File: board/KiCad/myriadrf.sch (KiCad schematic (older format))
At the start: 1 part, among them J1 FX10B_80S_8

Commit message: First pmod side wiring
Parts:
- J1: footprint FX10B_80S_8 -> (none)
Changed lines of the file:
@@
 LIBS:ice40_1k4k_tq144
 LIBS:myriad
+LIBS:pmod
+LIBS:LMS6002-Pmod-cache
 EELAYER 25 0
 EELAYER END
@@
 F 0 "J1" H 5600 6687 60  0000 C CNN
 F 1 "FX10B_80S_8" H 5580 6720 60  0001 C CNN
-F 2 "FX10B_80S_8" H 5590 6840 60  0001 C CNN
+F 2 "" H 5590 6840 60  0001 C CNN
 F 3 "" H 5600 3750 60  0000 C CNN
 F 4 "CONN RECEPT, 80POS, W/O, POST, SMD," H 5630 6950 60  0001 C CNN "Description"

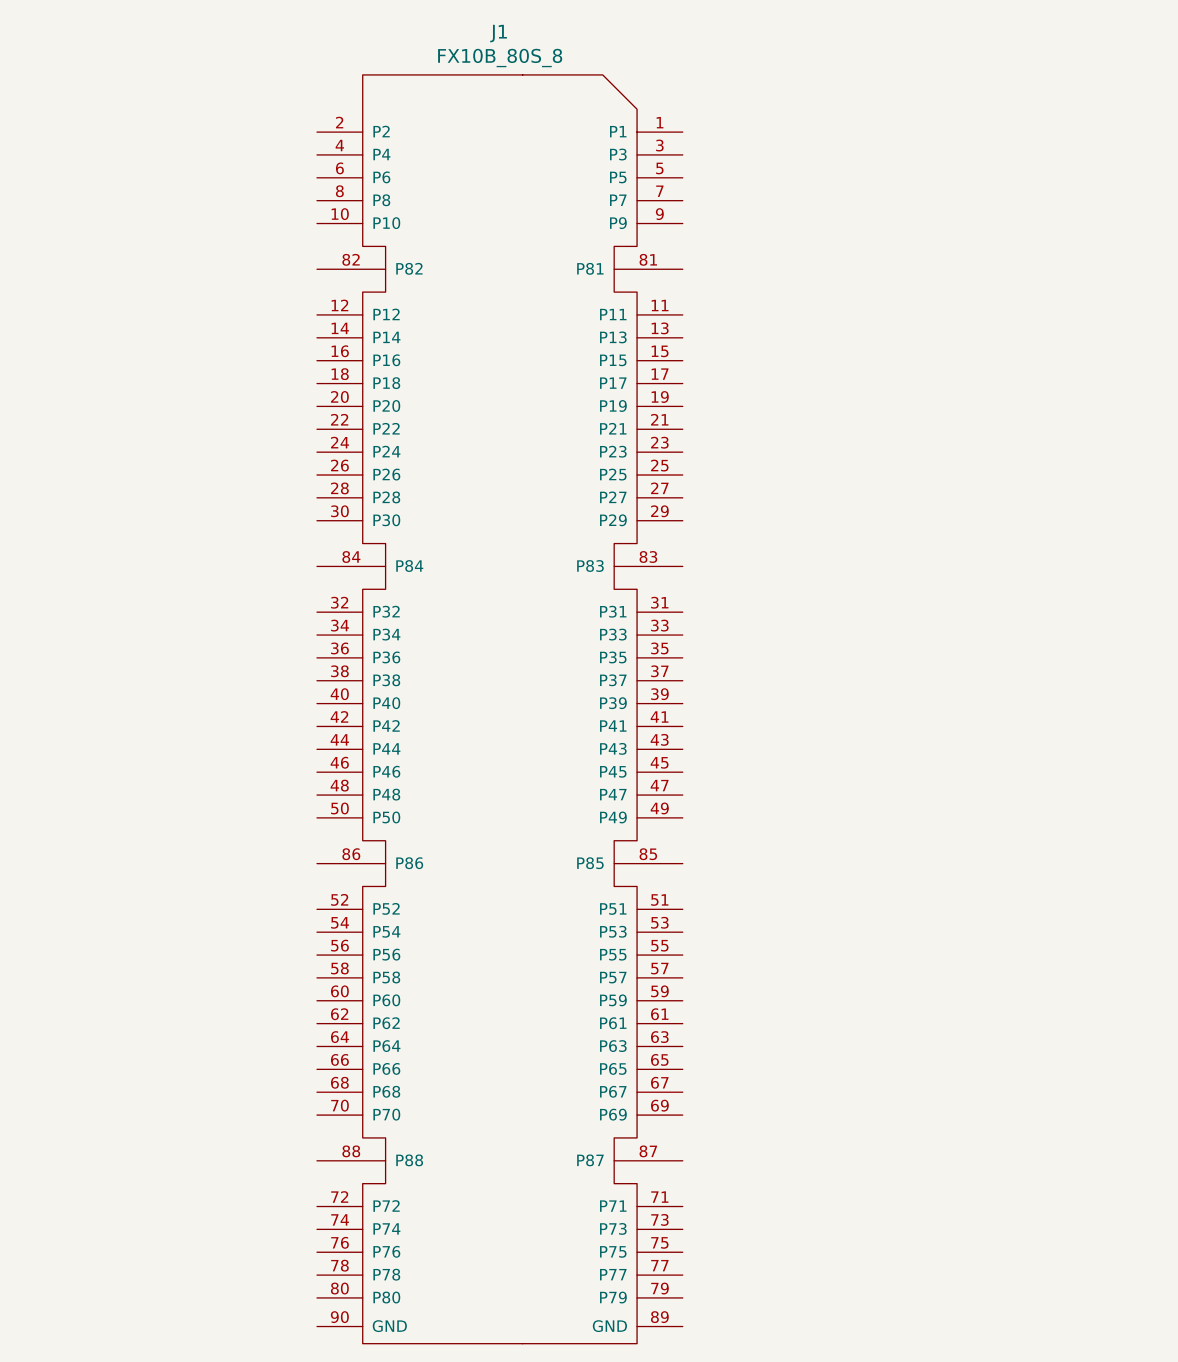
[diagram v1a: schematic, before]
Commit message: 1.2V power supply
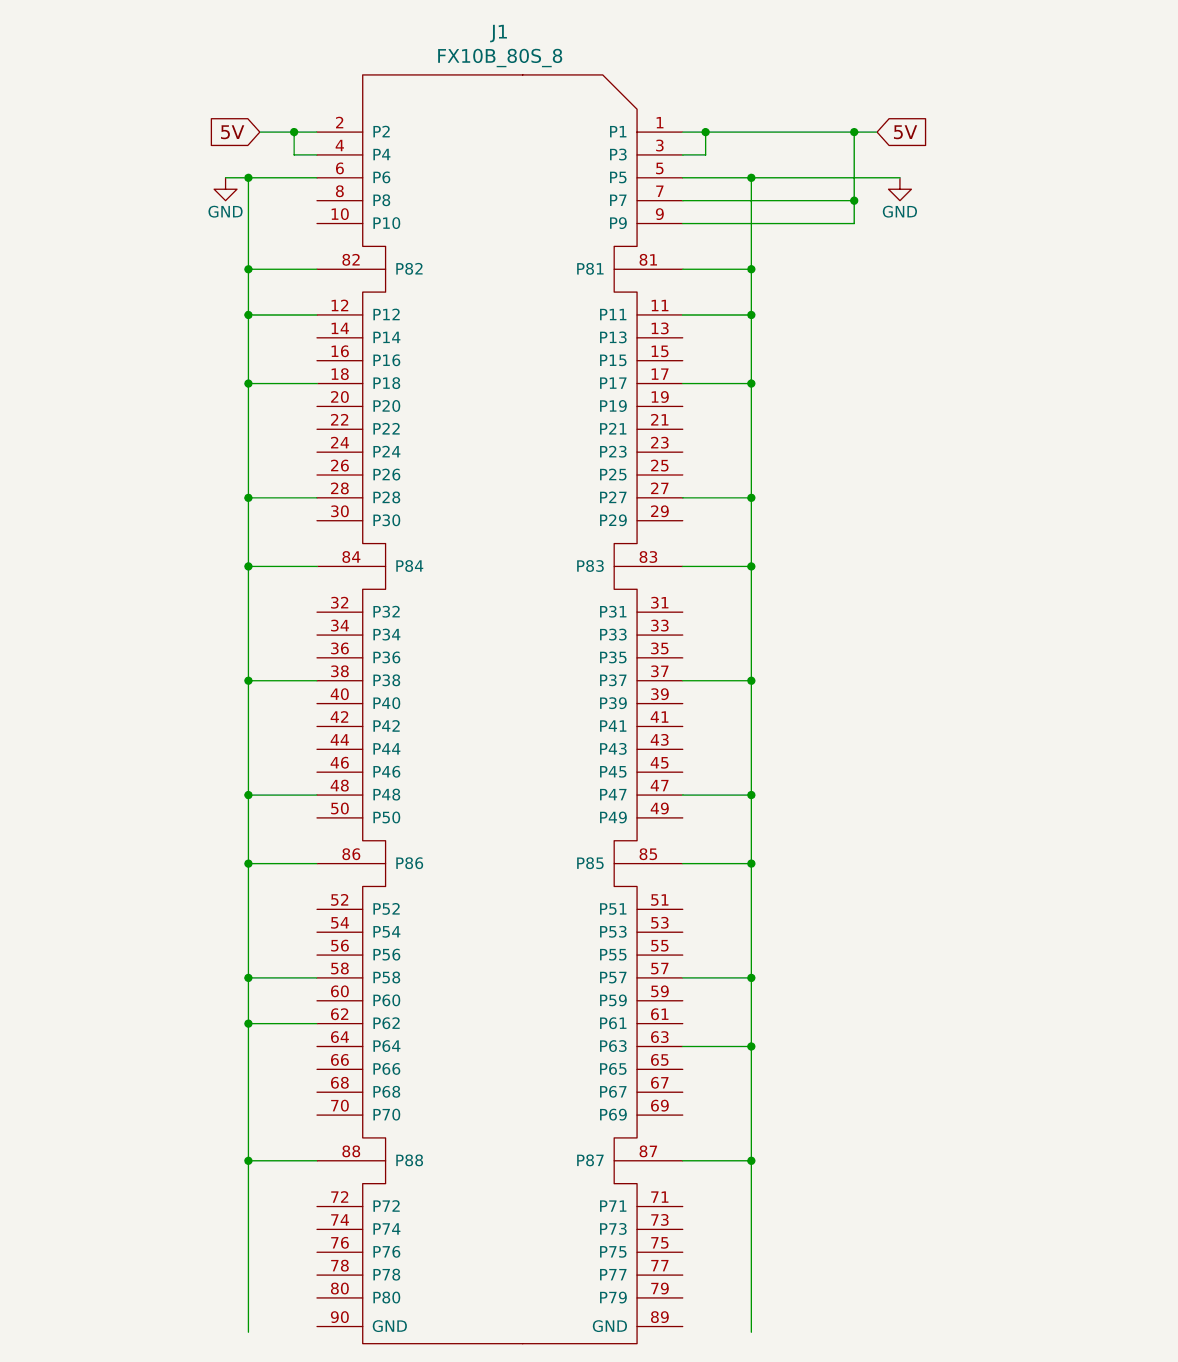
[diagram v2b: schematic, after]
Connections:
- net labels added: 5V, GND
- wire segments 0 -> 35
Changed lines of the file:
@@
 EESchema Schematic File Version 2
+LIBS:LMS6002-Pmod-rescue
 LIBS:power
 LIBS:device
@@
 $Descr A4 11693 8268
 encoding utf-8
-Sheet 4 4
+Sheet 4 5
 Title ""
 Date ""
@@
 	1    0    0    -1
 $EndComp
+Wire Wire Line
+	6400 1250 7250 1250
+Wire Wire Line
+	6500 1250 6500 1350
+Wire Wire Line
+	6500 1350 6400 1350
+Wire Wire Line
+	4550 1250 4800 1250
+Wire Wire Line
+	4700 1250 4700 1350
+Wire Wire Line
+	4700 1350 4800 1350
+Text GLabel 7250 1250 2    60   Input ~ 0
+5V
+Text GLabel 4550 1250 0    60   Input ~ 0
+5V
+Connection ~ 4700 1250
+Connection ~ 6500 1250
+$Comp
+L GND #PWR?
+U 1 1 56AB8EA2
+P 4400 1450
+F 0 "#PWR?" H 4400 1200 50  0001 C CNN
+F 1 "GND" H 4400 1300 50  0000 C CNN
+F 2 "" H 4400 1450 60  0000 C CNN
+F 3 "" H 4400 1450 60  0000 C CNN
+	1    4400 1450
+	1    0    0    -1
+$EndComp
+$Comp
+L GND #PWR?
+U 1 1 56AB8EB8
+P 7350 1450
+F 0 "#PWR?" H 7350 1200 50  0001 C CNN
+F 1 "GND" H 7350 1300 50  0000 C CNN
+F 2 "" H 7350 1450 60  0000 C CNN
+F 3 "" H 7350 1450 60  0000 C CNN
+	1    7350 1450
+	1    0    0    -1
+$EndComp
+Wire Wire Line
+	4400 1450 4800 1450
+Wire Wire Line
+	6400 1450 7350 1450
+Wire Wire Line
+	4800 1850 4500 1850
+Wire Wire Line
+	4500 1450 4500 6500
+Connection ~ 4500 1450
+Wire Wire Line
+	6400 1850 6700 1850
+Wire Wire Line
+	6700 1450 6700 6500
+Connection ~ 6700 1450
+Wire Wire Line
+	4500 3150 4800 3150
+Connection ~ 4500 1850
+Wire Wire Line
+	6400 3150 6700 3150
+Wire Wire Line
+	6700 4450 6400 4450
+Connection ~ 6700 3150
+Wire Wire Line
+	6700 5750 6400 5750
+Connection ~ 6700 4450
+Connection ~ 6700 5750
+Wire Wire Line
+	4500 4450 4800 4450
+Connection ~ 4500 3150
+Wire Wire Line
+	4500 5750 4800 5750
+Connection ~ 4500 4450
+Connection ~ 4500 5750
+Wire Wire Line
+	4800 2050 4500 2050
+Connection ~ 4500 2050
+Wire Wire Line
+	6400 2050 6700 2050
+Connection ~ 6700 2050
+Connection ~ 6700 1850
+Wire Wire Line
+	6400 1550 7150 1550
+Wire Wire Line
+	7150 1250 7150 1650
+Connection ~ 7150 1250
+Wire Wire Line
+	7150 1650 6400 1650
+Connection ~ 7150 1550
+Wire Wire Line
+	6400 2350 6700 2350
+Connection ~ 6700 2350
+Wire Wire Line
+	4800 2350 4500 2350
+Connection ~ 4500 2350
+Wire Wire Line
+	6400 2850 6700 2850
+Connection ~ 6700 2850
+Wire Wire Line
+	4800 2850 4500 2850
+Connection ~ 4500 2850
+Wire Wire Line
+	6400 3650 6700 3650
+Connection ~ 6700 3650
+Wire Wire Line
+	4800 3650 4500 3650
+Connection ~ 4500 3650
+Wire Wire Line
+	6400 4150 6700 4150
+Connection ~ 6700 4150
+Wire Wire Line
+	4800 4150 4500 4150
+Connection ~ 4500 4150
+Wire Wire Line
+	6400 4950 6700 4950
+Connection ~ 6700 4950
+Wire Wire Line
+	4800 4950 4500 4950
+Connection ~ 4500 4950
+Wire Wire Line
+	4800 5150 4500 5150
+Connection ~ 4500 5150
+Wire Wire Line
+	6400 5250 6700 5250
+Connection ~ 6700 5250
 $EndSCHEMATC

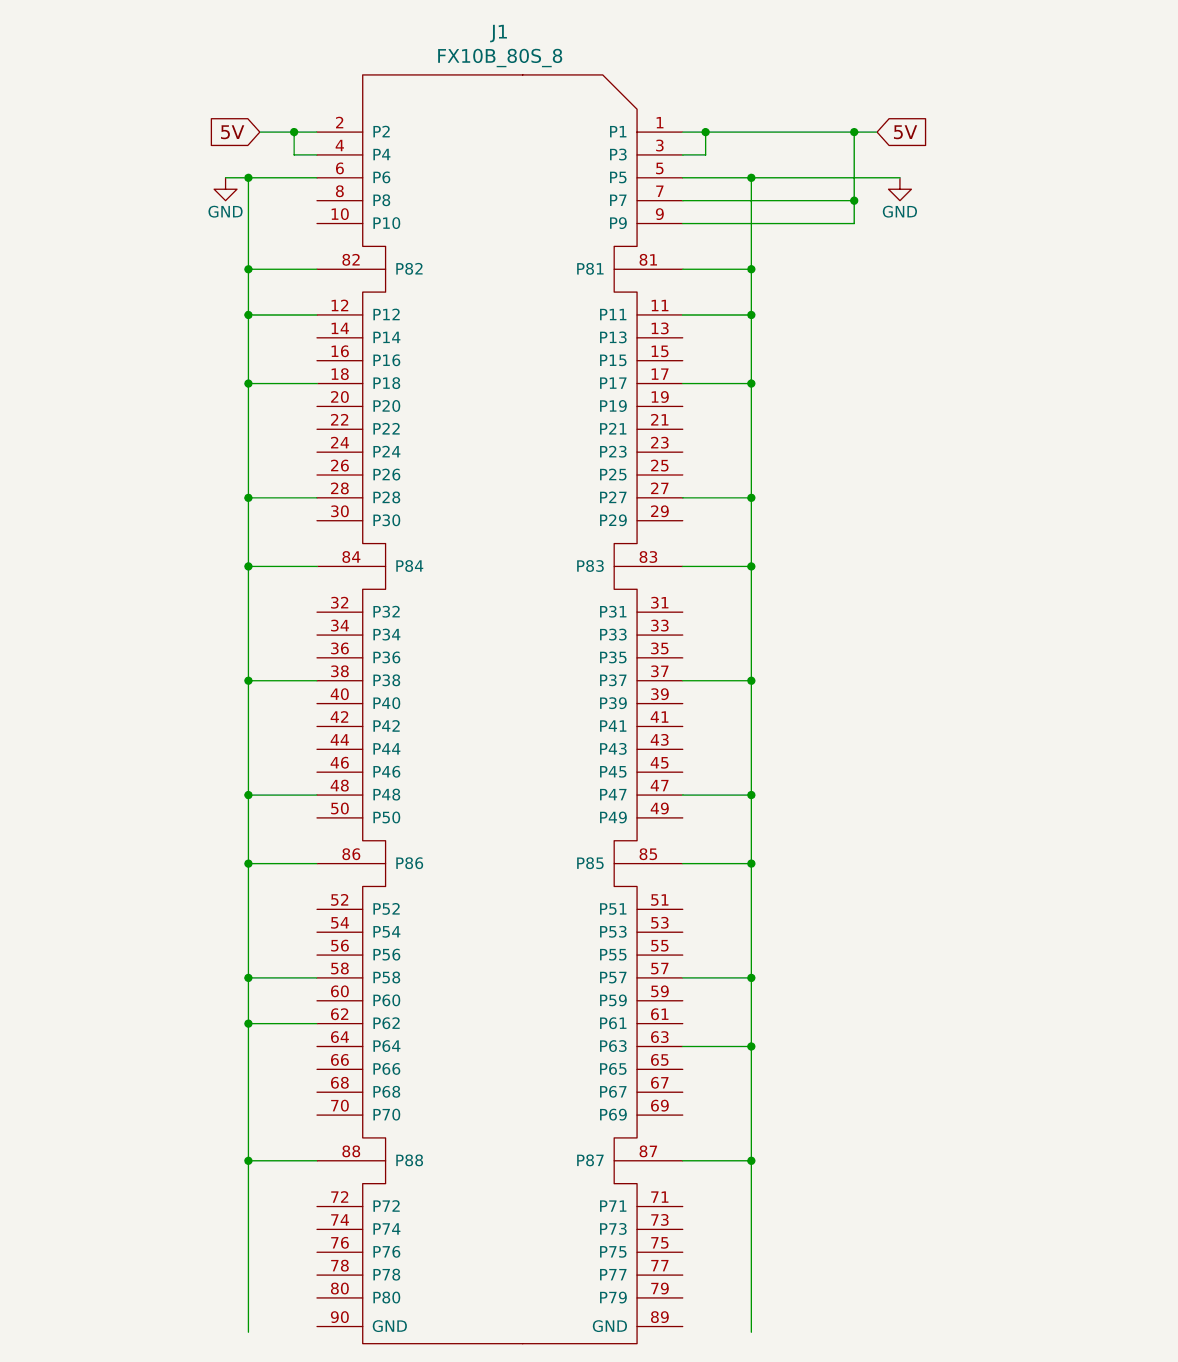
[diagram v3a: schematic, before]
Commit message: added DIQ1 bus to RFDIO
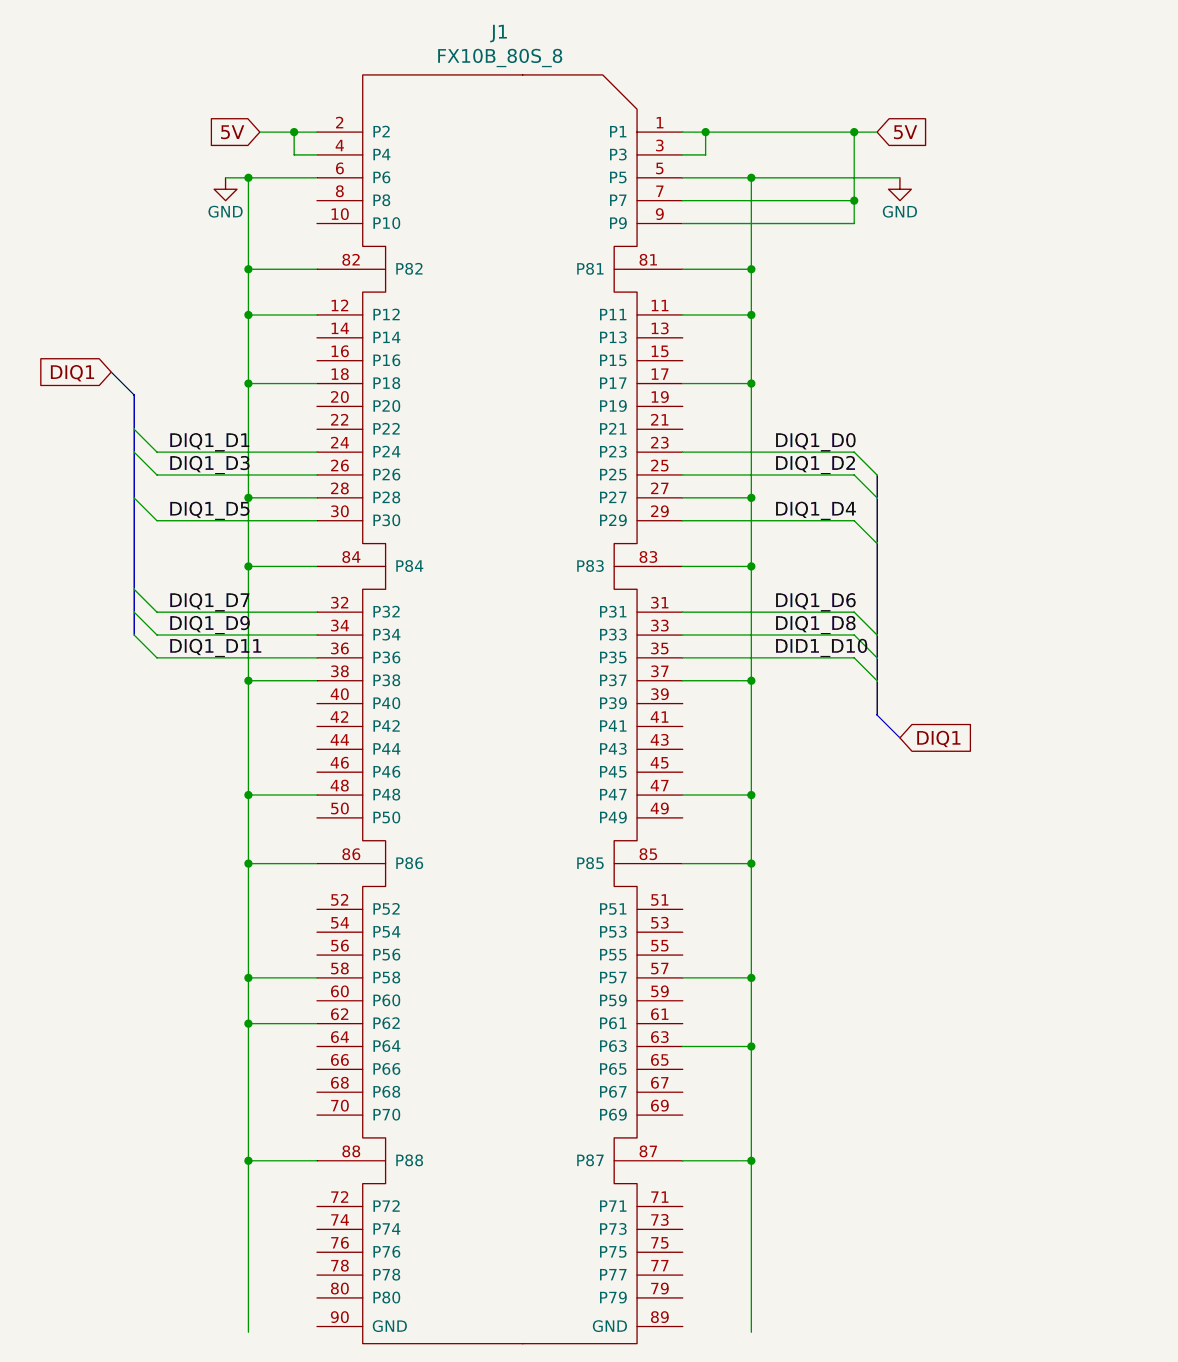
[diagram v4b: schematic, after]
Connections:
- net labels added: DID1_D10, DIQ1, DIQ1_D0, DIQ1_D1, DIQ1_D11, DIQ1_D2, DIQ1_D3, DIQ1_D4, DIQ1_D5, DIQ1_D6, DIQ1_D7, DIQ1_D8, DIQ1_D9
- wire segments 35 -> 47
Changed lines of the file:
@@
 	1    0    0    -1
 $EndComp
-Wire Wire Line
-	6400 1250 7250 1250
-Wire Wire Line
-	6500 1250 6500 1350
-Wire Wire Line
-	6500 1350 6400 1350
-Wire Wire Line
-	4550 1250 4800 1250
-Wire Wire Line
-	4700 1250 4700 1350
-Wire Wire Line
-	4700 1350 4800 1350
 Text GLabel 7250 1250 2    60   Input ~ 0
 5V
 Text GLabel 4550 1250 0    60   Input ~ 0
 5V
-Connection ~ 4700 1250
-Connection ~ 6500 1250
 $Comp
 L GND #PWR?
@@
 	1    0    0    -1
 $EndComp
+Entry Wire Line
+	7150 2650 7250 2750
+Entry Wire Line
+	7150 2750 7250 2850
+Entry Wire Line
+	7150 2950 7250 3050
+Entry Wire Line
+	7150 3350 7250 3450
+Entry Wire Line
+	7150 3450 7250 3550
+Entry Wire Line
+	7150 3550 7250 3650
+Wire Wire Line
+	6400 1250 7250 1250
+Wire Wire Line
+	6500 1250 6500 1350
+Wire Wire Line
+	6500 1350 6400 1350
+Wire Wire Line
+	4550 1250 4800 1250
+Wire Wire Line
+	4700 1250 4700 1350
+Wire Wire Line
+	4700 1350 4800 1350
+Connection ~ 4700 1250
+Connection ~ 6500 1250
 Wire Wire Line
 	4400 1450 4800 1450
@@
 	6400 5250 6700 5250
 Connection ~ 6700 5250
+Wire Wire Line
+	6400 2650 7150 2650
+Wire Wire Line
+	6400 2750 7150 2750
+Wire Wire Line
+	4800 2650 4100 2650
+Wire Wire Line
+	4800 2750 4100 2750
+Wire Wire Line
+	6400 2950 7150 2950
+Wire Wire Line
+	4800 2950 4100 2950
+Wire Wire Line
+	6400 3350 7150 3350
+Wire Wire Line
+	6400 3450 7150 3450
+Wire Wire Line
+	6400 3550 7150 3550
+Wire Wire Line
+	4800 3350 4100 3350
+Wire Wire Line
+	4800 3450 4100 3450
+Wire Wire Line
+	4800 3550 4100 3550
+Wire Bus Line
+	7250 2750 7250 3800
+Entry Wire Line
+	4000 2550 4100 2650
+Entry Wire Line
+	4000 2650 4100 2750
+Entry Wire Line
+	4000 2850 4100 2950
+Entry Wire Line
+	4000 3250 4100 3350
+Entry Wire Line
+	4000 3350 4100 3450
+Entry Wire Line
+	4000 3450 4100 3550
+Wire Bus Line
+	4000 3450 4000 2400
+Text Label 6800 2650 0    60   ~ 0
+DIQ1_D0
+Text Label 6800 2750 0    60   ~ 0
+DIQ1_D2
+Text Label 6800 2950 0    60   ~ 0
+DIQ1_D4
+Text Label 6800 3350 0    60   ~ 0
+DIQ1_D6
+Text Label 6800 3450 0    60   ~ 0
+DIQ1_D8
+Text Label 6800 3550 0    60   ~ 0
+DID1_D10
+Text Label 4150 2650 0    60   ~ 0
+DIQ1_D1
+Text Label 4150 2750 0    60   ~ 0
+DIQ1_D3
+Text Label 4150 2950 0    60   ~ 0
+DIQ1_D5
+Text Label 4150 3350 0    60   ~ 0
+DIQ1_D7
+Text Label 4150 3450 0    60   ~ 0
+DIQ1_D9
+Text Label 4150 3550 0    60   ~ 0
+DIQ1_D11
+Text GLabel 7350 3900 2    60   Input ~ 0
+DIQ1
+Text GLabel 3900 2300 0    60   Input ~ 0
+DIQ1
+Entry Bus Bus
+	7250 3800 7350 3900
+Entry Bus Bus
+	3900 2300 4000 2400
 $EndSCHEMATC

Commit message: fixed RFDIO supply pins
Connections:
- wire segments 47 -> 44
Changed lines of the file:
@@
 Connection ~ 6700 2050
 Connection ~ 6700 1850
-Wire Wire Line
-	6400 1550 7150 1550
-Wire Wire Line
-	7150 1250 7150 1650
 Connection ~ 7150 1250
 Wire Wire Line
-	7150 1650 6400 1650
-Connection ~ 7150 1550
-Wire Wire Line
 	6400 2350 6700 2350

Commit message: DIQ1 Bus added
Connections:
- net labels added: RXEN, RXIQSEL, TXEN, TXIQSEL
- wire segments 44 -> 48
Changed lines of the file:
@@
 Wire Wire Line
 	4800 1850 4500 1850
-Wire Wire Line
-	4500 1450 4500 6500
 Connection ~ 4500 1450
 Wire Wire Line
 	6400 1850 6700 1850
-Wire Wire Line
-	6700 1450 6700 6500
 Connection ~ 6700 1450
 Wire Wire Line
@@
 Entry Bus Bus
 	3900 2300 4000 2400
+Wire Wire Line
+	6400 2450 7150 2450
+Text GLabel 7150 2450 2    60   Input ~ 0
+TXIQSEL
+Wire Wire Line
+	6400 3750 7850 3750
+Text GLabel 7850 3750 2    60   Input ~ 0
+RXIQSEL
+Wire Wire Line
+	4500 5750 4500 1450
+Wire Wire Line
+	6700 5750 6700 1450
+Wire Wire Line
+	4800 6350 4500 6350
+Text GLabel 4500 6350 0    60   Input ~ 0
+RXEN
+Wire Wire Line
+	6400 6350 7200 6350
+Text GLabel 7200 6350 2    60   Input ~ 0
+TXEN
 $EndSCHEMATC
